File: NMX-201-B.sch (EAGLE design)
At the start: 61 parts, among them IC1 A4983TOP, IC2 A4983TOP, IC3 A4983TOP, J1 MOLEX-4-RAPRO-CONNECTOR, J2 MOLEX-4-RAPRO-CONNECTOR, J3 MOLEX-4-RAPRO-CONNECTOR, U1 CADJ, U2 CADJ, U3 MOUNT-HOLE3.2, U4 MOUNT-HOLE3.2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

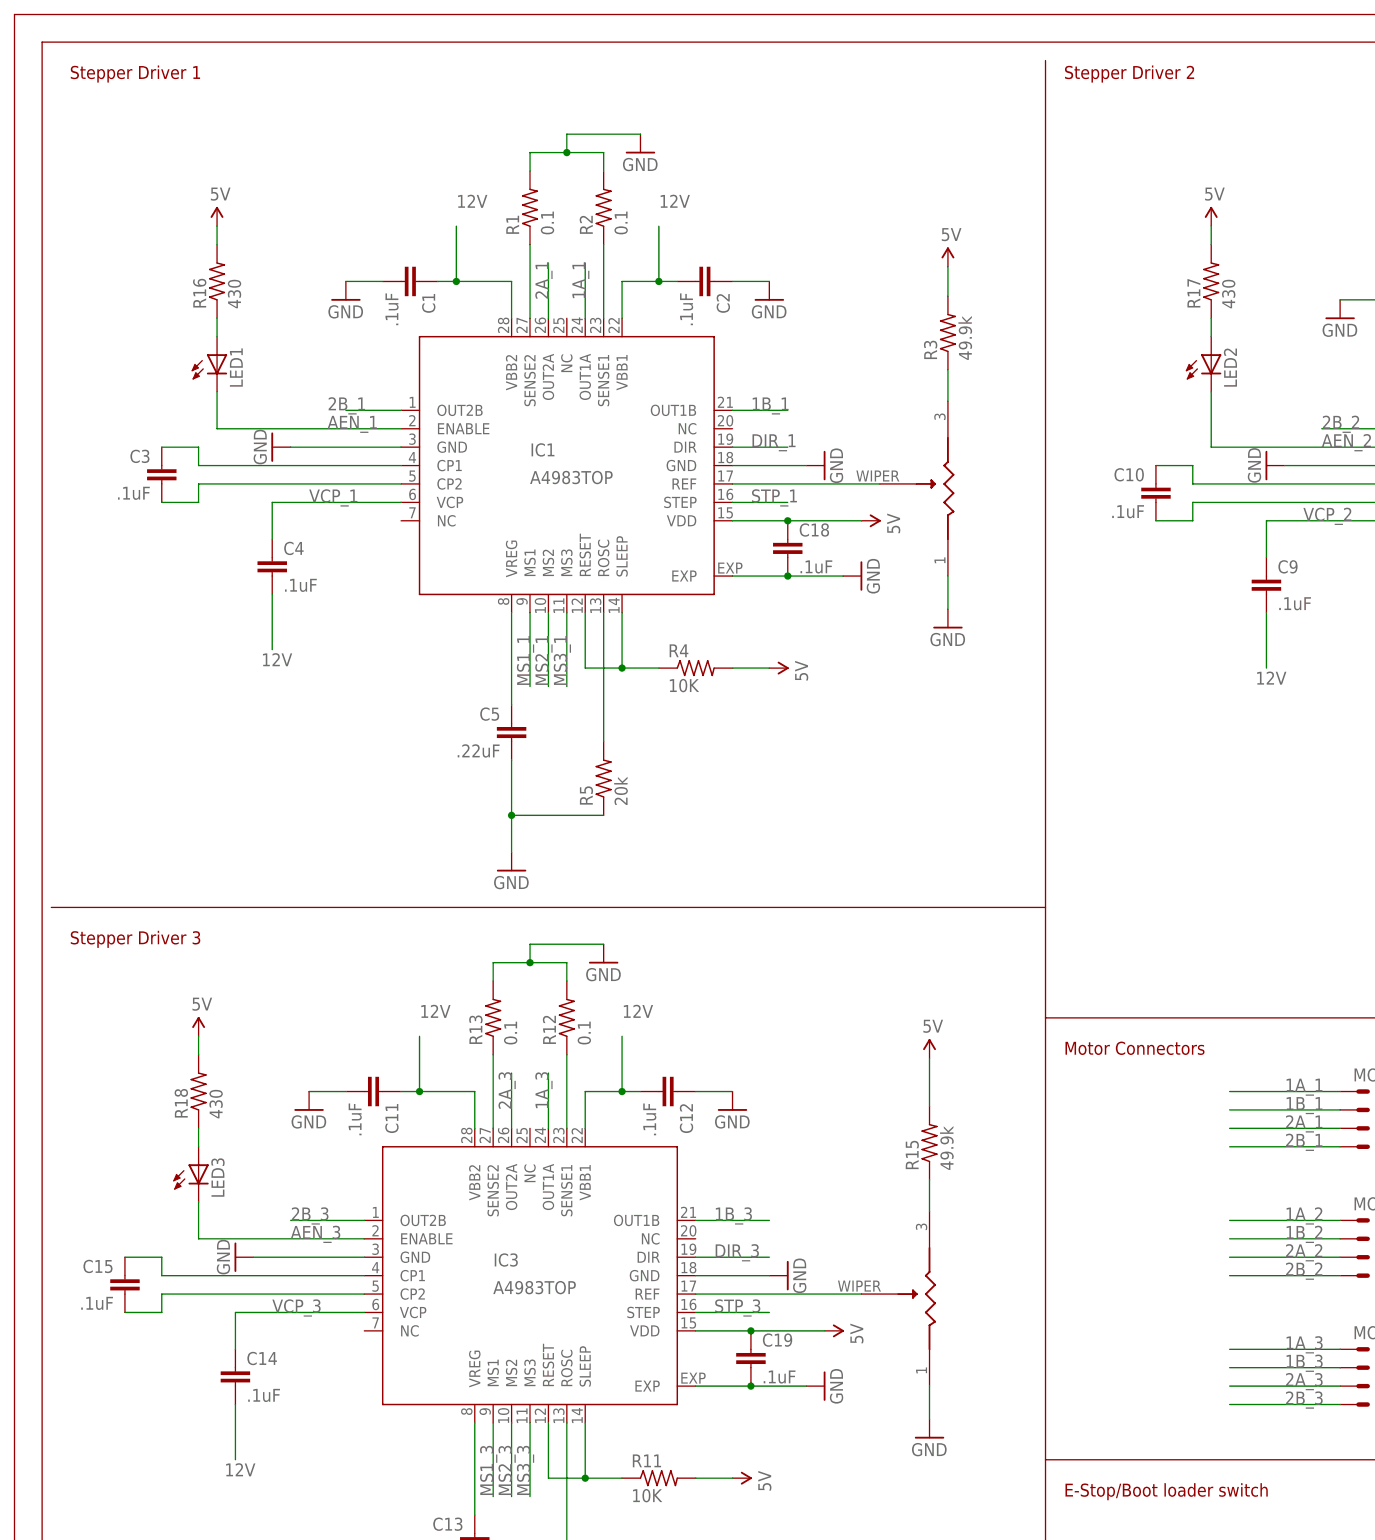
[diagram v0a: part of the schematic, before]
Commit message: Added DIP switches and increased LED resistor vals
NMX 201-B:
- Added switches to allow users to turn off motor movement indicator
LEDs.
- Changed R16, R17, R19 to 14k resistances in order to reduce LED
brightness.
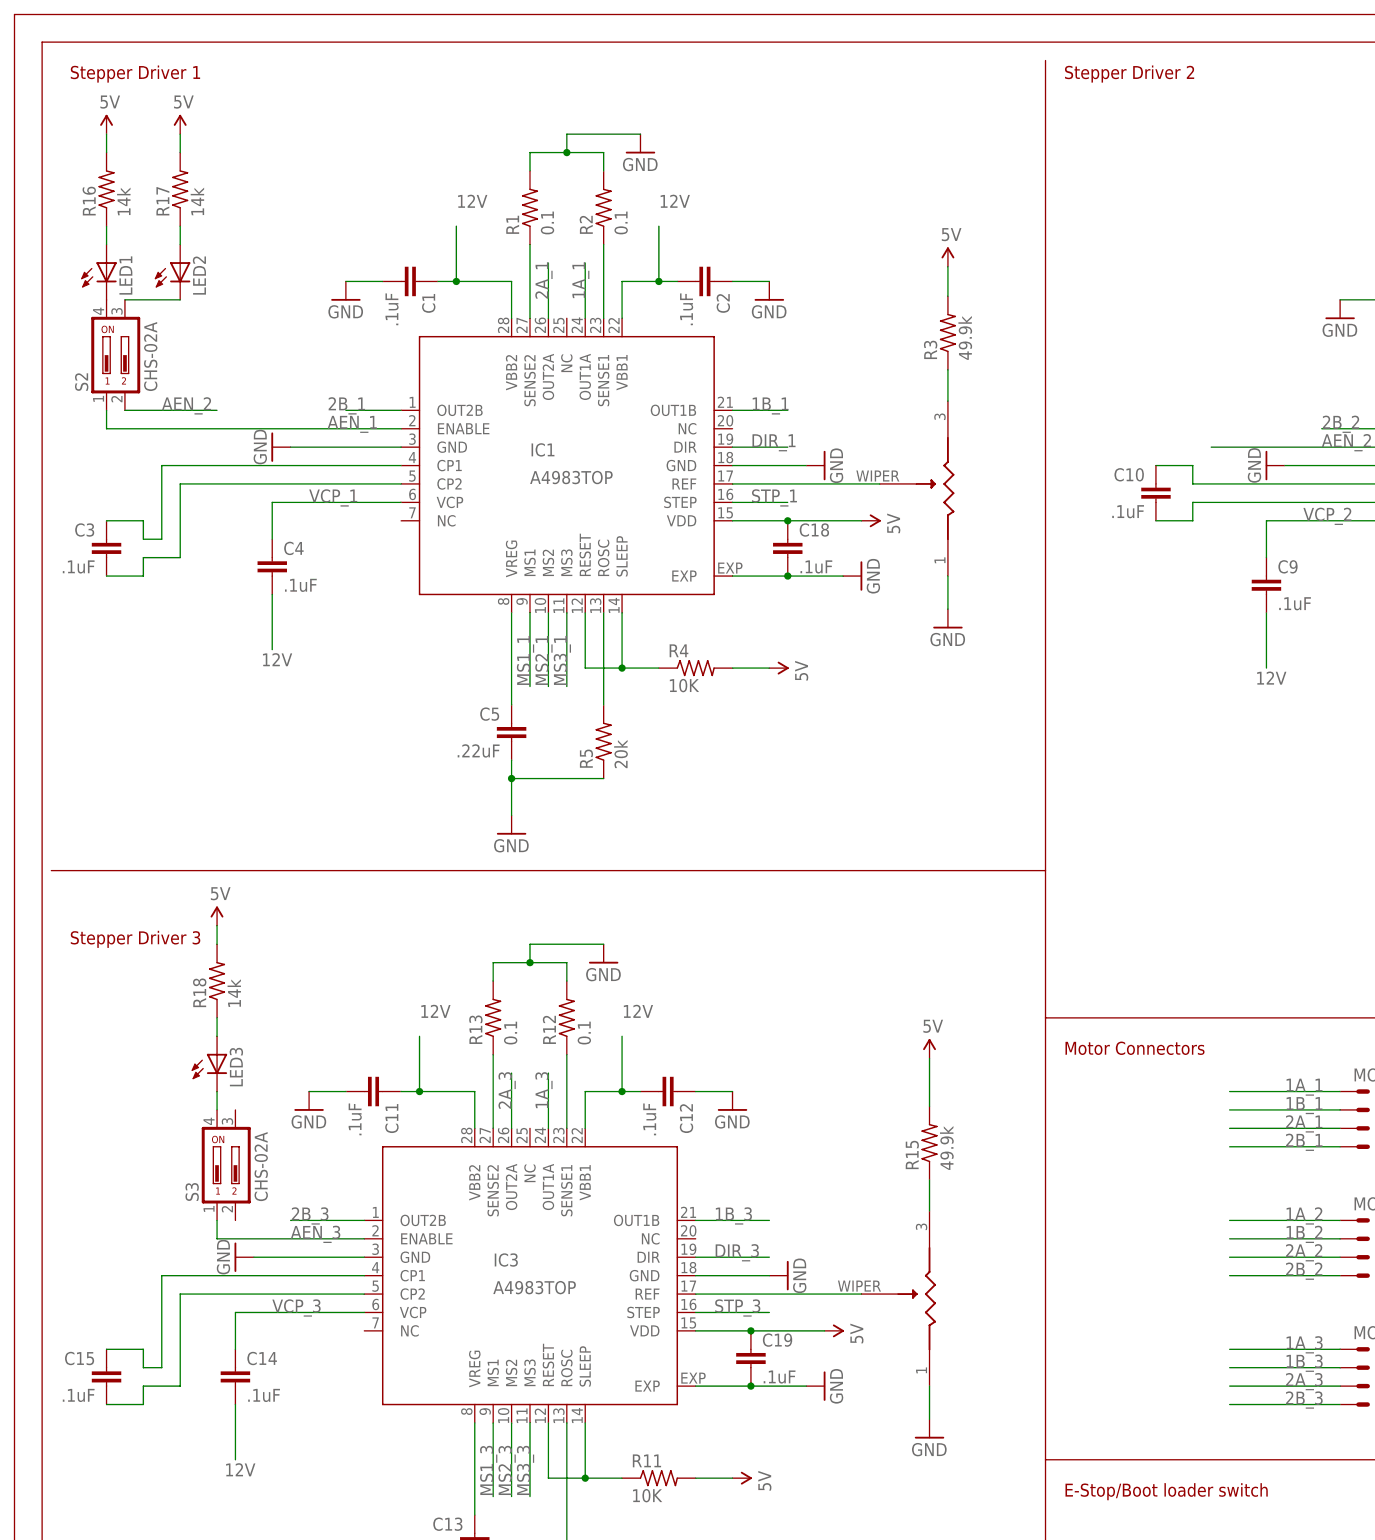
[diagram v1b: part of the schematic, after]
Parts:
- added S2, S3: CHS-02A, switch-copal:CHS-02A
- R16, R17, R18: value 430 -> 14k; MPN RC0402FR-07430RL -> RC0402FR-0714KL
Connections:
- new net N$16: LED1.C, S2.4
- new net N$18: LED2.C, S2.3
- new net N$19: LED3.C, S3.4
- net AEN_1: now also S2.1; no longer LED1.C
- net AEN_2: now also S2.2; no longer LED2.C
- net AEN_3: now also S3.1; no longer LED3.C
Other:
- moved on the sheet: C15, C3, LED1, LED2, LED3, R16, R17, R18, R5
